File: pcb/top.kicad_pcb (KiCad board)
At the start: 2 copper layers, 186 x 28 mm, 63 parts, among them J1 Conn_01x01, J10 Conn_01x01, J11 Conn_01x01, J2 Conn_01x01, J3 Conn_01x06, J4 Conn_01x01, J5 Conn_01x01, J6 Conn_01x01, J7 Conn_01x01, J8 Conn_01x01, J9 Conn_01x01, Q1 2N7002, Q2 2N7002, Q3 2N7002, Q4 2N7002, U1 L78L05_SOT89, U2 PIC12F629-ISN

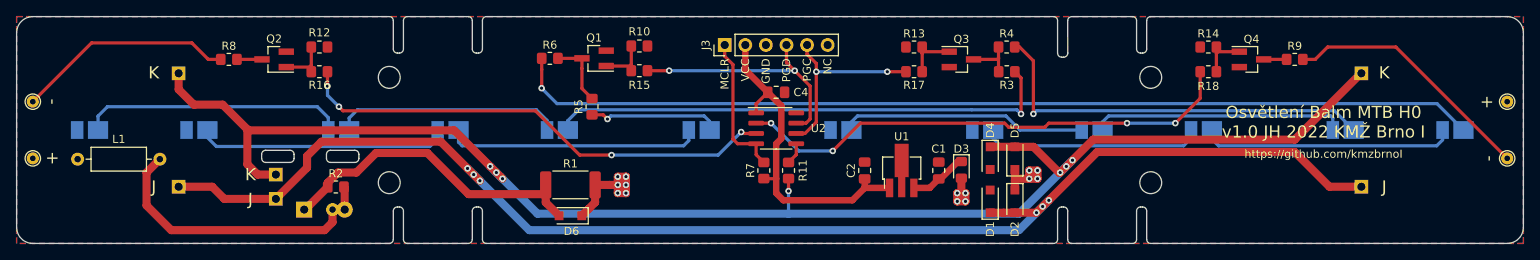
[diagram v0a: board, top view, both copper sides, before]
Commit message: Migrate to KiCad 6.
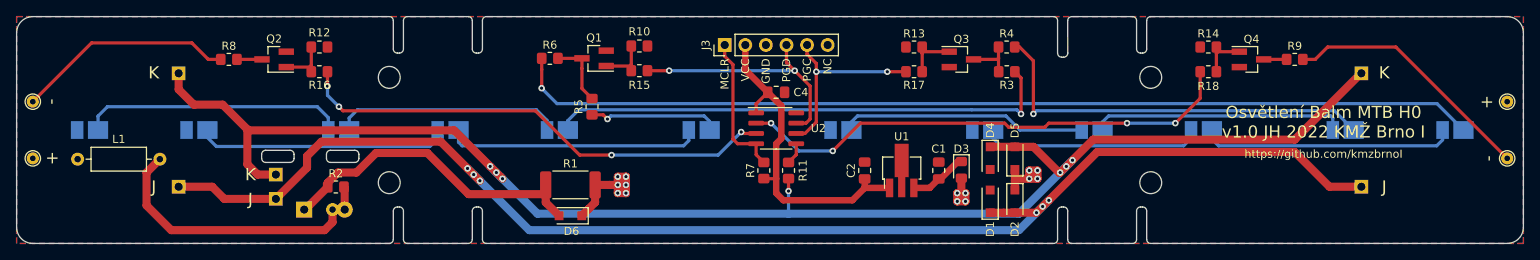
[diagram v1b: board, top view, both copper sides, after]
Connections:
- J3 pad 6: (no net) -> unconnected-(J3-Pad6)
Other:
- net class Default removed

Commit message: Add OSHW logo.
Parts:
- added REF**: OSHW-Logo_11.4x12mm_SilkScreen, Symbol:OSHW-Logo_11.4x12mm_SilkScreen, F.Cu at (131.8, 91.0)
- added REF**: WEEE-Logo_8.4x12mm_SilkScreen, Symbol:WEEE-Logo_8.4x12mm_SilkScreen, F.Cu at (181.5, 89.8)
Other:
- board text added: "https://github.com/kmzbrnoI https://kmz-brno.cz/"
- board text removed: "https://github.com/kmzbrnoI"

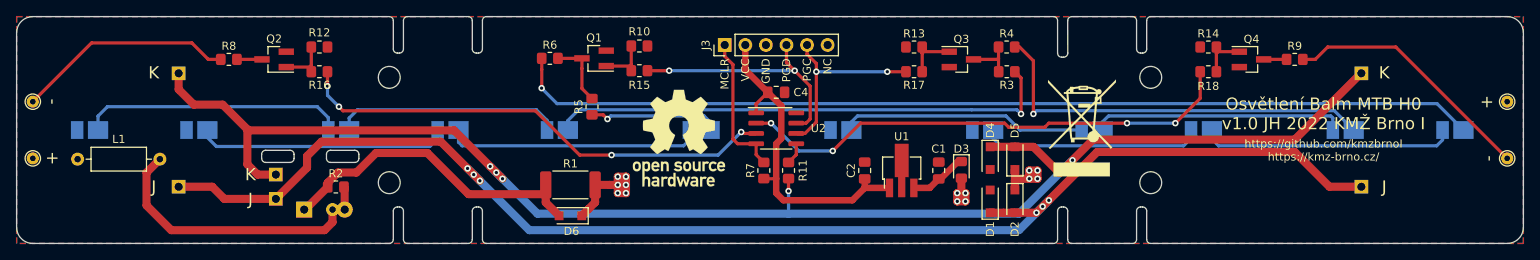
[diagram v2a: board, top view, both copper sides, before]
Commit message: Top: add 100n capacitor on input.
To filter DCC edges (causing transistors to open).
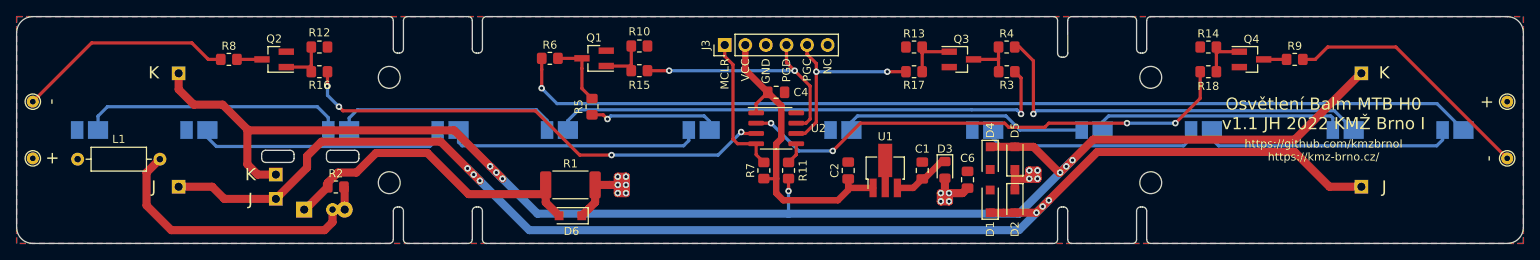
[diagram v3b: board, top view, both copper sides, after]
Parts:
- removed REF**: OSHW-Logo_11.4x12mm_SilkScreen, Symbol:OSHW-Logo_11.4x12mm_SilkScreen
- removed REF**: WEEE-Logo_8.4x12mm_SilkScreen, Symbol:WEEE-Logo_8.4x12mm_SilkScreen
- added C6: 100n, Capacitor_SMD:C_0805_2012Metric_Pad1.18x1.45mm_HandSolder, F.Cu at (167.4, 96.1)
- moved C1 2.03 mm to (161.8, 95.0)
- moved C2 2.03 mm to (152.7, 95.0)
- moved U1 2.03 mm to (157.2, 95.0)
- moved D3 2.03 mm to (164.6, 94.9)
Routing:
- net +15V: track 34.7 -> 37.3 mm
- net VCC: track 41.4 -> 39.5 mm
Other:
- board text added: "Osvětlení Balm MTB H0 v1.1 JH 2022 KMŽ Brno I"
- board text removed: "Osvětlení Balm MTB H0 v1.0 JH 2022 KMŽ Brno I"

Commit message: Change front transistors 10k → 47k.
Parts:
- R8, R9: value 10k -> 47k
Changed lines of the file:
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@@
     (descr "Resistor SMD 0805 (2012 Metric), square (rectangular) end terminal, IPC_7351 nominal with elongated pad for handsoldering. (Body size source: IPC-SM-782 page 72, https://www.pcb-3d.com/wordpress/wp-content/uploads/ipc-sm-782a_amendment_1_and_2.pdf), generated with kicad-footprint-generator")
     (tags "resistor handsolder")
-    (property "LCSC" "C17414")
+    (property "LCSC" "C17713")
     (property "Sheetfile" "top.kicad_sch")
     (property "Sheetname" "")
@@
       (effects (font (size 1 1) (thickness 0.15)))
     )
-    (fp_text value "10k" (at 0 1.65) (layer "F.Fab")
+    (fp_text value "47k" (at 0 1.65) (layer "F.Fab")
       (effects (font (size 1 1) (thickness 0.15)))
     )
@@
     (descr "Resistor SMD 0805 (2012 Metric), square (rectangular) end terminal, IPC_7351 nominal with elongated pad for handsoldering. (Body size source: IPC-SM-782 page 72, https://www.pcb-3d.com/wordpress/wp-content/uploads/ipc-sm-782a_amendment_1_and_2.pdf), generated with kicad-footprint-generator")
     (tags "resistor handsolder")
-    (property "LCSC" "C17414")
+    (property "LCSC" "C17713")
     (property "Sheetfile" "top.kicad_sch")
     (property "Sheetname" "")
@@
       (effects (font (size 1 1) (thickness 0.15)))
     )
-    (fp_text value "10k" (at 0 1.65) (layer "F.Fab")
+    (fp_text value "47k" (at 0 1.65) (layer "F.Fab")
       (effects (font (size 1 1) (thickness 0.15)))
     )

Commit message: Change capacitor-discharge resistor to 22k.
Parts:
- R2: value 2k2 -> 22k
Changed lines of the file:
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@@
     (descr "Resistor SMD 0805 (2012 Metric), square (rectangular) end terminal, IPC_7351 nominal with elongated pad for handsoldering. (Body size source: IPC-SM-782 page 72, https://www.pcb-3d.com/wordpress/wp-content/uploads/ipc-sm-782a_amendment_1_and_2.pdf), generated with kicad-footprint-generator")
     (tags "resistor handsolder")
-    (property "LCSC" "C17520")
+    (property "LCSC" "C17560")
     (property "Sheetfile" "top.kicad_sch")
     (property "Sheetname" "")
@@
       (effects (font (size 1 1) (thickness 0.15)))
     )
-    (fp_text value "2k2" (at 0 1.65) (layer "F.Fab")
+    (fp_text value "22k" (at 0 1.65) (layer "F.Fab")
       (effects (font (size 1 1) (thickness 0.15)))
     )

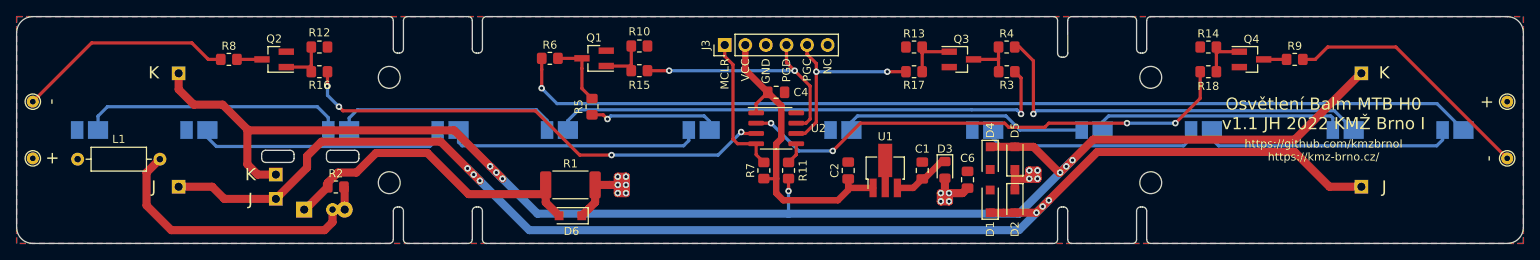
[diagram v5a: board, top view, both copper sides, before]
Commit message: Use schottky diodes on rectifier & capacitor.
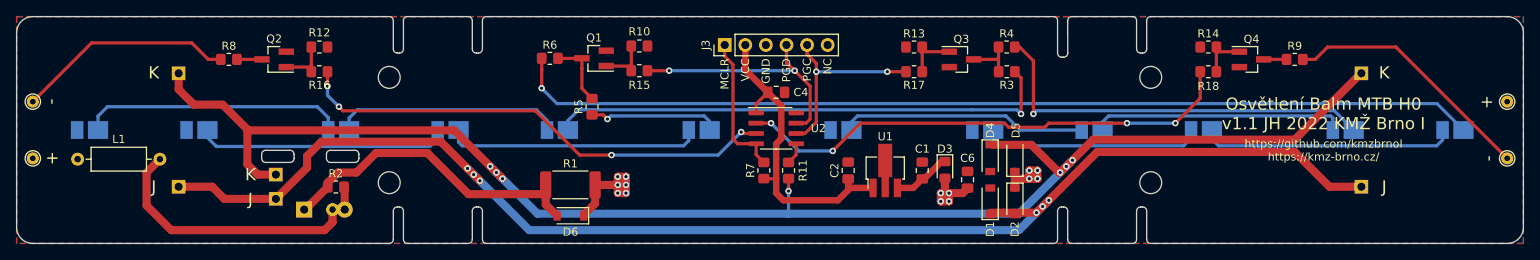
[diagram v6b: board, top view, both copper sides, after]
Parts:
- D1, D2, D4, D5, D6: value 1N4007 -> 1N5819; footprint Diode_SMD:D_SOD-123F -> Diode_SMD:D_SOD-123
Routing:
- net +15V: track 37.3 -> 36.7 mm

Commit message: Reposition corridor LEDs to be in the middle of corridor.
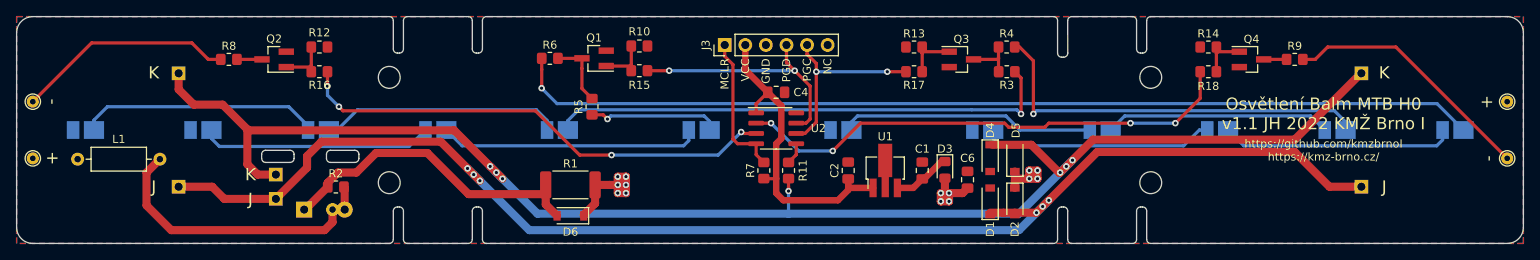
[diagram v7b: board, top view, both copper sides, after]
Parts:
- moved D11 2.50 mm to (87.5, 90.0)
- moved D14 2.00 mm to (198.5, 90.0)
- moved D13 1.50 mm to (102.0, 90.0)
- moved D12 1.00 mm to (184.0, 90.0)
- moved D16 1.00 mm to (213.0, 90.0)
- moved D7 0.50 mm to (58.5, 90.0)
- moved D9 0.50 mm to (73.0, 90.0)
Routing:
- net Net-(D12-Pad1): track 31.3 -> 27.9 mm
- net Net-(D11-Pad2): track 32.7 -> 29.8 mm
- net Net-(D14-Pad1): track 31.5 -> 28.8 mm
- net Net-(D13-Pad2): track 31.3 -> 28.7 mm
- net Net-(D11-Pad1): track 28.1 -> 29.7 mm
- net Net-(D10-Pad1): track 27.3 -> 28.7 mm
- net Net-(D12-Pad2): track 30.4 -> 31.4 mm
- net Net-(D13-Pad1): track 31.7 -> 32.3 mm

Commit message: Change order of LEDs to 2-2-2-2-2-2.
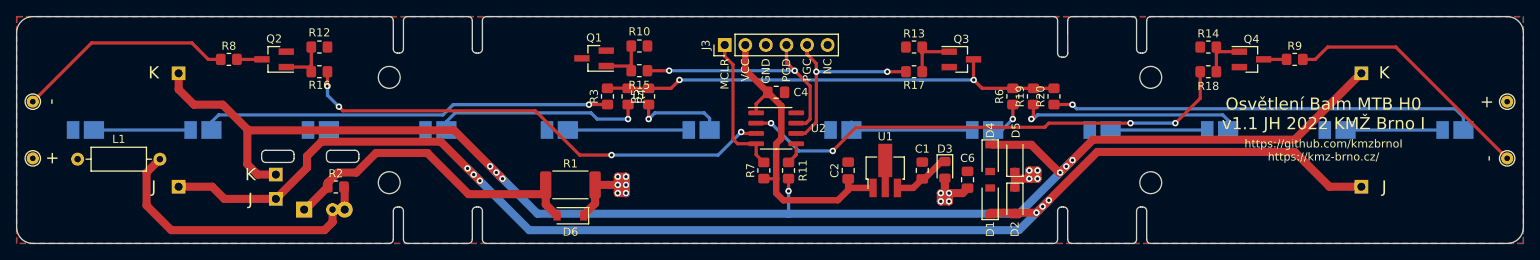
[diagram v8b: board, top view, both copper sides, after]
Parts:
- added R19: 10k, Resistor_SMD:R_0805_2012Metric_Pad1.20x1.40mm_HandSolder, F.Cu at (175.5, 85.9)
- added R20: 10k, Resistor_SMD:R_0805_2012Metric_Pad1.20x1.40mm_HandSolder, F.Cu at (178.1, 85.9)
- moved R6 57.3 mm to (173.0, 85.9), turned to 90 degrees
- moved R3 49.4 mm to (122.9, 85.9), turned to 90 degrees
- moved R4 47.1 mm to (125.5, 85.9), turned to 90 degrees
- moved R5 7.10 mm to (128.0, 85.9)
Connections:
- D10 pad 1: Net-(D10-Pad1) -> Net-(R6-Pad1)
- D10 pad 2: +15V -> Net-(D8-Pad1)
- D11 pad 2: Net-(D11-Pad2) -> +15V
- D12 pad 2: Net-(D12-Pad2) -> +15V
- D13 pad 1: Net-(D13-Pad1) -> Net-(R4-Pad1)
- D13 pad 2: Net-(D13-Pad2) -> Net-(D11-Pad1)
- D14 pad 1: Net-(D14-Pad1) -> Net-(R19-Pad1)
- D14 pad 2: Net-(D10-Pad1) -> Net-(D12-Pad1)
- D15 pad 2: Net-(D11-Pad1) -> +15V
- D16 pad 2: Net-(D12-Pad1) -> +15V
- D17 pad 2: Net-(D13-Pad1) -> Net-(D15-Pad1)
- D18 pad 1: Net-(D18-Pad1) -> Net-(R20-Pad1)
- D18 pad 2: Net-(D14-Pad1) -> Net-(D16-Pad1)
- D7 pad 1: Net-(D11-Pad2) -> Net-(D7-Pad1)
- D8 pad 1: Net-(D12-Pad2) -> Net-(D8-Pad1)
- D9 pad 1: Net-(D13-Pad2) -> Net-(D9-Pad1)
- D9 pad 2: +15V -> Net-(D7-Pad1)
- Q1 pad 3: Net-(Q1-Pad3) -> unconnected-(Q1-Pad3)
- Q3 pad 3: Net-(Q3-Pad3) -> Net-(R3-Pad2)
- R3 pad 1: Net-(D15-Pad1) -> Net-(D9-Pad1)
- R3 pad 2: Net-(Q3-Pad3) -> Net-(R3-Pad2)
- R4 pad 1: Net-(D16-Pad1) -> Net-(R4-Pad1)
- R4 pad 2: Net-(Q3-Pad3) -> Net-(R3-Pad2)
- R5 pad 2: Net-(Q1-Pad3) -> Net-(R3-Pad2)
- R6 pad 1: Net-(D18-Pad1) -> Net-(R6-Pad1)
- R6 pad 2: Net-(Q1-Pad3) -> Net-(R3-Pad2)
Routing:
- net Net-(D18-Pad1): track 119.6 -> 0.00 mm, vias 1 -> 0
- net Net-(R3-Pad2): track 0.00 -> 58.5 mm, vias 0 -> 2
- net Net-(R20-Pad1): track 0.00 -> 52.8 mm, vias 0 -> 1
- net Net-(D9-Pad1): track 0.00 -> 50.8 mm, vias 0 -> 1
- net Net-(D15-Pad1): track 63.4 -> 14.9 mm, vias 1 -> 0
- net Net-(D16-Pad1): track 49.8 -> 12.0 mm, vias 1 -> 0
- net Net-(D13-Pad1): track 32.3 -> 0.00 mm
- net Net-(D12-Pad2): track 31.4 -> 0.00 mm
- net Net-(D11-Pad2): track 29.8 -> 0.00 mm
- net Net-(D14-Pad1): track 28.8 -> 0.00 mm
- net Net-(D13-Pad2): track 28.7 -> 0.00 mm
- net Net-(D10-Pad1): track 28.7 -> 0.00 mm
- net Net-(R19-Pad1): track 0.00 -> 27.9 mm, vias 0 -> 1
- net Net-(R4-Pad1): track 0.00 -> 26.0 mm, vias 0 -> 1
- net Net-(D11-Pad1): track 29.7 -> 11.9 mm
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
